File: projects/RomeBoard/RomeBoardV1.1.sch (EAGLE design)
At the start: 27 parts, among them J1 HEADER-5, J2 RASPBERRY-PI-HEADER, M1 2N7000, M2 2N7000, M3 2N7000, U1 LM1084IT-ADJ

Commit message: fixing air wire + updating library
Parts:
- M1, M2, M3: value 2N7000 -> ZVN4424A; device BrownSpaceEngineering:2N7000 -> BrownSpaceEngineering:ZVN4424A
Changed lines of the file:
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@@
 <part name="R7" library="passives" deviceset="RESISTOR" device="-PTH0.4" value="147R"/>
 <part name="GND6" library="supply1" deviceset="GND" device=""/>
-<part name="M1" library="BrownSpaceEngineering" deviceset="2N7000" device=""/>
-<part name="M2" library="BrownSpaceEngineering" deviceset="2N7000" device=""/>
-<part name="M3" library="BrownSpaceEngineering" deviceset="2N7000" device=""/>
+<part name="M1" library="BrownSpaceEngineering" deviceset="ZVN4424A" device=""/>
+<part name="M2" library="BrownSpaceEngineering" deviceset="ZVN4424A" device=""/>
+<part name="M3" library="BrownSpaceEngineering" deviceset="ZVN4424A" device=""/>
 <part name="R8" library="passives" deviceset="RESISTOR" device="-PTH0.4" value="10K"/>
 <part name="U1" library="BrownSpaceEngineering" deviceset="LM1084IT-ADJ" device=""/>
@@
 <instance part="R7" gate="G$1" x="162.56" y="48.26" rot="R90"/>
 <instance part="GND6" gate="1" x="127" y="17.78"/>
-<instance part="M1" gate="G$1" x="86.36" y="33.02"/>
-<instance part="M2" gate="G$1" x="121.92" y="33.02"/>
-<instance part="M3" gate="G$1" x="157.48" y="33.02"/>
+<instance part="M1" gate="G$1" x="86.36" y="33.02" smashed="yes">
+<attribute name="NAME" x="83.82" y="35.56" size="1.778" layer="97"/>
+<attribute name="VALUE" x="78.74" y="27.94" size="1.778" layer="97"/>
+</instance>
+<instance part="M2" gate="G$1" x="121.92" y="33.02" smashed="yes">
+<attribute name="NAME" x="119.38" y="35.56" size="1.778" layer="97"/>
+<attribute name="VALUE" x="114.3" y="27.94" size="1.778" layer="97"/>
+</instance>
+<instance part="M3" gate="G$1" x="157.48" y="33.02" smashed="yes">
+<attribute name="NAME" x="154.94" y="35.56" size="1.778" layer="97"/>
+<attribute name="VALUE" x="149.86" y="27.94" size="1.778" layer="97"/>
+</instance>
 </instances>
 <busses>

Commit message: Adding fan connectors to board, increasing board size, re-routing some stuff
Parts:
- added C4, C5: 0.1uF, BrownSpaceEngineering:CAP5MM-THRU-HOLE
- added FAN1, FAN2: FAD1-04010BBLW11, BrownSpaceEngineering:FAD1-04010BBLW11
- R2: value 450R -> 282R
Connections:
- net GND: now also C4.P$2, C5.P$2, FAN1.+\, FAN2.-
- net VIN: now also C4.P$1, C5.P$1, FAN1.-, FAN2.+\
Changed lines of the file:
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@@
 <part name="R8" library="passives" deviceset="RESISTOR" device="-PTH0.4" value="10K"/>
 <part name="U1" library="BrownSpaceEngineering" deviceset="LM1084IT-ADJ" device=""/>
-<part name="R2" library="passives" deviceset="RESISTOR" device="-PTH0.4" value="450R"/>
+<part name="R2" library="passives" deviceset="RESISTOR" device="-PTH0.4" value="282R"/>
 <part name="R1" library="passives" deviceset="RESISTOR" device="-PTH0.4" value="150R"/>
 <part name="GND2" library="supply1" deviceset="GND" device=""/>
@@
 <part name="C3" library="resistor" library_urn="urn:adsk.eagle:library:348" deviceset="CPOL-EU" device="E5-13" package3d_urn="urn:adsk.eagle:package:25855/1" value="150uF"/>
 <part name="D1" library="BrownSpaceEngineering" deviceset="1N4002" device=""/>
+<part name="FAN1" library="BrownSpaceEngineering" deviceset="FAD1-04010BBLW11" device=""/>
+<part name="FAN2" library="BrownSpaceEngineering" deviceset="FAD1-04010BBLW11" device=""/>
+<part name="GND7" library="supply1" deviceset="GND" device=""/>
+<part name="C4" library="BrownSpaceEngineering" deviceset="CAP" device="5MM-THRU-HOLE" value="0.1uF"/>
+<part name="C5" library="BrownSpaceEngineering" deviceset="CAP" device="5MM-THRU-HOLE" value="0.1uF"/>
 </parts>
 <sheets>
@@
 </segment>
 </net>
+</nets>
+</sheet>
+<sheet>
+<description>Fans</description>
+<plain>
+</plain>
+<instances>
+<instance part="FAN1" gate="G$1" x="48.26" y="48.26" smashed="yes" rot="R90">
+<attribute name="NAME" x="38.608" y="54.356" size="1.778" layer="95"/>
+<attribute name="VALUE" x="56.388" y="38.1" size="1.778" layer="96" rot="R90"/>
+</instance>
+<instance part="FAN2" gate="G$1" x="83.82" y="48.26" smashed="yes" rot="R270">
+<attribute name="NAME" x="93.472" y="57.404" size="1.778" layer="95" rot="R180"/>
+<attribute name="VALUE" x="75.692" y="58.42" size="1.778" layer="96" rot="R270"/>
+</instance>
+<instance part="GND7" gate="1" x="66.04" y="15.24"/>
+<instance part="C4" gate="G$1" x="33.02" y="45.72"/>
+<instance part="C5" gate="G$1" x="99.06" y="45.72"/>
+</instances>
+<busses>
+</busses>
+<nets>
+<net name="VIN" class="0">
+<segment>
+<pinref part="FAN1" gate="G$1" pin="-"/>
+<wire x1="48.26" y1="58.42" x2="48.26" y2="60.96" width="0.1524" layer="91"/>
+<wire x1="48.26" y1="60.96" x2="48.26" y2="71.12" width="0.1524" layer="91"/>
+<wire x1="48.26" y1="71.12" x2="30.48" y2="71.12" width="0.1524" layer="91"/>
+<wire x1="48.26" y1="71.12" x2="83.82" y2="71.12" width="0.1524" layer="91"/>
+<wire x1="83.82" y1="71.12" x2="83.82" y2="60.96" width="0.1524" layer="91"/>
+<junction x="48.26" y="71.12"/>
+<label x="33.02" y="71.12" size="1.778" layer="95"/>
+<pinref part="C4" gate="G$1" pin="P$1"/>
+<wire x1="33.02" y1="50.8" x2="33.02" y2="60.96" width="0.1524" layer="91"/>
+<wire x1="33.02" y1="60.96" x2="48.26" y2="60.96" width="0.1524" layer="91"/>
+<junction x="48.26" y="60.96"/>
+<pinref part="C5" gate="G$1" pin="P$1"/>
+<wire x1="99.06" y1="50.8" x2="99.06" y2="60.96" width="0.1524" layer="91"/>
+<wire x1="99.06" y1="60.96" x2="83.82" y2="60.96" width="0.1524" layer="91"/>
+<pinref part="FAN2" gate="G$1" pin="+\"/>
+<wire x1="83.82" y1="58.42" x2="83.82" y2="60.96" width="0.1524" layer="91"/>
+<junction x="83.82" y="60.96"/>
+</segment>
+</net>
+<net name="GND" class="0">
+<segment>
+<pinref part="FAN1" gate="G$1" pin="+\"/>
+<wire x1="48.26" y1="38.1" x2="48.26" y2="35.56" width="0.1524" layer="91"/>
+<wire x1="48.26" y1="35.56" x2="48.26" y2="22.86" width="0.1524" layer="91"/>
+<wire x1="48.26" y1="22.86" x2="66.04" y2="22.86" width="0.1524" layer="91"/>
+<wire x1="66.04" y1="22.86" x2="83.82" y2="22.86" width="0.1524" layer="91"/>
+<wire x1="83.82" y1="22.86" x2="83.82" y2="35.56" width="0.1524" layer="91"/>
+<pinref part="GND7" gate="1" pin="GND"/>
+<wire x1="66.04" y1="17.78" x2="66.04" y2="22.86" width="0.1524" layer="91"/>
+<junction x="66.04" y="22.86"/>
+<pinref part="C4" gate="G$1" pin="P$2"/>
+<wire x1="33.02" y1="43.18" x2="33.02" y2="35.56" width="0.1524" layer="91"/>
+<wire x1="33.02" y1="35.56" x2="48.26" y2="35.56" width="0.1524" layer="91"/>
+<junction x="48.26" y="35.56"/>
+<pinref part="C5" gate="G$1" pin="P$2"/>
+<wire x1="99.06" y1="43.18" x2="99.06" y2="35.56" width="0.1524" layer="91"/>
+<wire x1="99.06" y1="35.56" x2="83.82" y2="35.56" width="0.1524" layer="91"/>
+<pinref part="FAN2" gate="G$1" pin="-"/>
+<wire x1="83.82" y1="38.1" x2="83.82" y2="35.56" width="0.1524" layer="91"/>
+<junction x="83.82" y="35.56"/>
+</segment>
+</net>

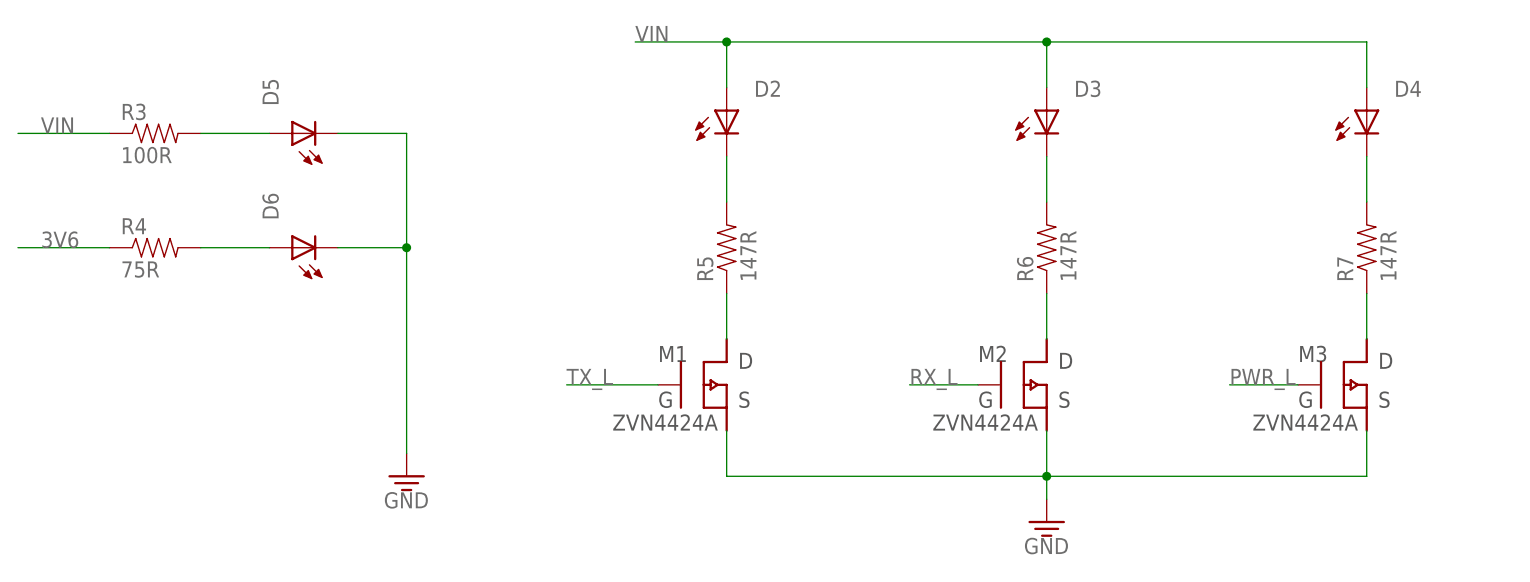
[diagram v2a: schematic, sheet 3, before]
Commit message: Adding gate pulldowns for NPNs
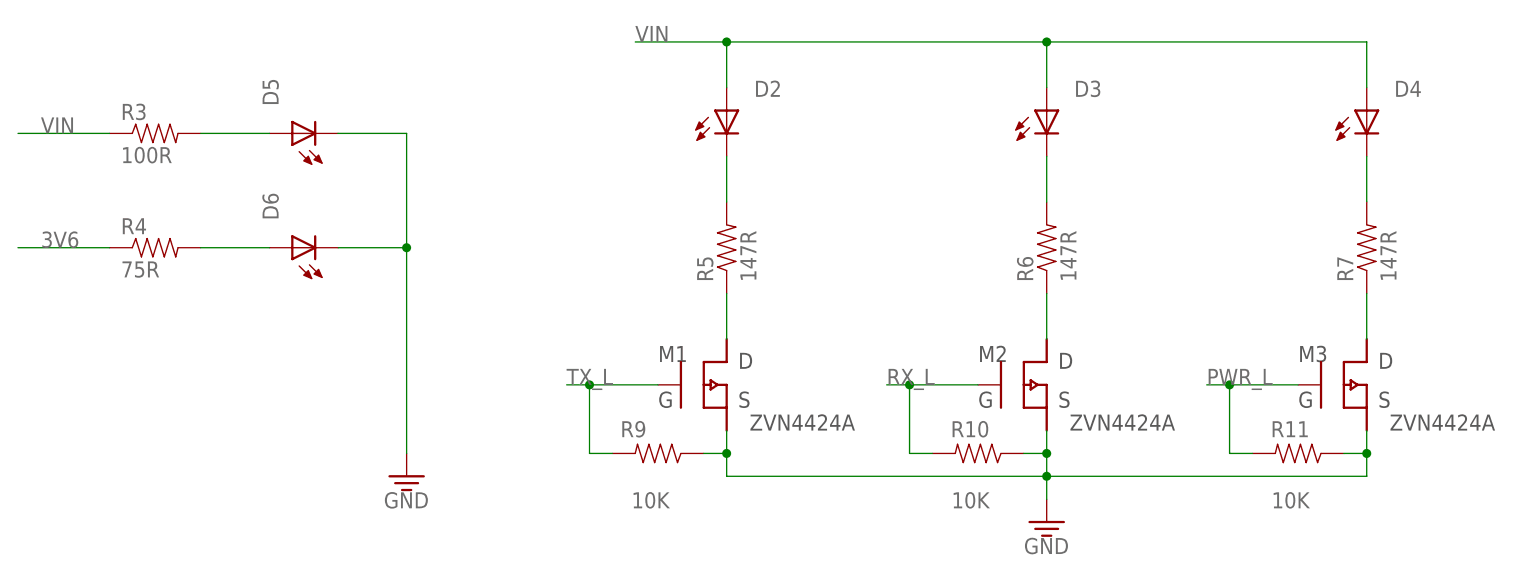
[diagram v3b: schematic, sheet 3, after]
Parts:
- added R10, R11, R9: 10K, passives:RESISTOR-PTH0.4
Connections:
- net GND: now also R10.1, R11.1, R9.1
- net PWR_L: now also R11.2
- net RX_L: now also R10.2
- net TX_L: now also R9.2
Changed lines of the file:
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@@
 <part name="C4" library="BrownSpaceEngineering" deviceset="CAP" device="5MM-THRU-HOLE" value="0.1uF"/>
 <part name="C5" library="BrownSpaceEngineering" deviceset="CAP" device="5MM-THRU-HOLE" value="0.1uF"/>
+<part name="R9" library="passives" deviceset="RESISTOR" device="-PTH0.4" value="10K"/>
+<part name="R10" library="passives" deviceset="RESISTOR" device="-PTH0.4" value="10K"/>
+<part name="R11" library="passives" deviceset="RESISTOR" device="-PTH0.4" value="10K"/>
 </parts>
 <sheets>
@@
 <instance part="M1" gate="G$1" x="86.36" y="33.02" smashed="yes">
 <attribute name="NAME" x="83.82" y="35.56" size="1.778" layer="97"/>
-<attribute name="VALUE" x="78.74" y="27.94" size="1.778" layer="97"/>
+<attribute name="VALUE" x="93.98" y="27.94" size="1.778" layer="97"/>
 </instance>
 <instance part="M2" gate="G$1" x="121.92" y="33.02" smashed="yes">
 <attribute name="NAME" x="119.38" y="35.56" size="1.778" layer="97"/>
-<attribute name="VALUE" x="114.3" y="27.94" size="1.778" layer="97"/>
+<attribute name="VALUE" x="129.54" y="27.94" size="1.778" layer="97"/>
 </instance>
 <instance part="M3" gate="G$1" x="157.48" y="33.02" smashed="yes">
 <attribute name="NAME" x="154.94" y="35.56" size="1.778" layer="97"/>
-<attribute name="VALUE" x="149.86" y="27.94" size="1.778" layer="97"/>
+<attribute name="VALUE" x="165.1" y="27.94" size="1.778" layer="97"/>
+</instance>
+<instance part="R9" gate="G$1" x="83.82" y="25.4" smashed="yes" rot="R180">
+<attribute name="NAME" x="82.55" y="28.9814" size="1.778" layer="95" rot="R180"/>
+<attribute name="VALUE" x="85.09" y="21.082" size="1.778" layer="96" rot="R180"/>
+</instance>
+<instance part="R10" gate="G$1" x="119.38" y="25.4" smashed="yes" rot="R180">
+<attribute name="NAME" x="120.65" y="28.9814" size="1.778" layer="95" rot="R180"/>
+<attribute name="VALUE" x="120.65" y="21.082" size="1.778" layer="96" rot="R180"/>
+</instance>
+<instance part="R11" gate="G$1" x="154.94" y="25.4" smashed="yes" rot="R180">
+<attribute name="NAME" x="156.21" y="28.9814" size="1.778" layer="95" rot="R180"/>
+<attribute name="VALUE" x="156.21" y="21.082" size="1.778" layer="96" rot="R180"/>
 </instance>
 </instances>
@@
 <wire x1="127" y1="22.86" x2="162.56" y2="22.86" width="0.1524" layer="91"/>
 <pinref part="M1" gate="G$1" pin="S"/>
-<wire x1="91.44" y1="27.94" x2="91.44" y2="22.86" width="0.1524" layer="91"/>
+<wire x1="91.44" y1="27.94" x2="91.44" y2="25.4" width="0.1524" layer="91"/>
 <pinref part="M2" gate="G$1" pin="S"/>
-<wire x1="127" y1="27.94" x2="127" y2="22.86" width="0.1524" layer="91"/>
+<wire x1="91.44" y1="25.4" x2="91.44" y2="22.86" width="0.1524" layer="91"/>
+<wire x1="127" y1="27.94" x2="127" y2="25.4" width="0.1524" layer="91"/>
 <pinref part="M3" gate="G$1" pin="S"/>
-<wire x1="162.56" y1="27.94" x2="162.56" y2="22.86" width="0.1524" layer="91"/>
+<wire x1="127" y1="25.4" x2="127" y2="22.86" width="0.1524" layer="91"/>
+<wire x1="162.56" y1="27.94" x2="162.56" y2="25.4" width="0.1524" layer="91"/>
+<pinref part="R10" gate="G$1" pin="1"/>
+<wire x1="162.56" y1="25.4" x2="162.56" y2="22.86" width="0.1524" layer="91"/>
+<wire x1="124.46" y1="25.4" x2="127" y2="25.4" width="0.1524" layer="91"/>
+<junction x="127" y="25.4"/>
+<pinref part="R9" gate="G$1" pin="1"/>
+<wire x1="88.9" y1="25.4" x2="91.44" y2="25.4" width="0.1524" layer="91"/>
+<junction x="91.44" y="25.4"/>
+<pinref part="R11" gate="G$1" pin="1"/>
+<wire x1="160.02" y1="25.4" x2="162.56" y2="25.4" width="0.1524" layer="91"/>
+<junction x="162.56" y="25.4"/>
 </segment>
 </net>
@@
 <segment>
 <pinref part="M1" gate="G$1" pin="G"/>
-<wire x1="83.82" y1="33.02" x2="73.66" y2="33.02" width="0.1524" layer="91"/>
+<wire x1="83.82" y1="33.02" x2="76.2" y2="33.02" width="0.1524" layer="91"/>
 <label x="73.66" y="33.02" size="1.778" layer="95"/>
+<pinref part="R9" gate="G$1" pin="2"/>
+<wire x1="78.74" y1="25.4" x2="76.2" y2="25.4" width="0.1524" layer="91"/>
+<wire x1="76.2" y1="25.4" x2="76.2" y2="33.02" width="0.1524" layer="91"/>
+<wire x1="76.2" y1="33.02" x2="73.66" y2="33.02" width="0.1524" layer="91"/>
+<junction x="76.2" y="33.02"/>
 </segment>
 </net>
@@
 <pinref part="M2" gate="G$1" pin="G"/>
 <wire x1="119.38" y1="33.02" x2="111.76" y2="33.02" width="0.1524" layer="91"/>
-<label x="111.76" y="33.02" size="1.778" layer="95"/>
+<label x="109.22" y="33.02" size="1.778" layer="95"/>
+<pinref part="R10" gate="G$1" pin="2"/>
+<wire x1="111.76" y1="33.02" x2="109.22" y2="33.02" width="0.1524" layer="91"/>
+<wire x1="114.3" y1="25.4" x2="111.76" y2="25.4" width="0.1524" layer="91"/>
+<wire x1="111.76" y1="25.4" x2="111.76" y2="33.02" width="0.1524" layer="91"/>
+<junction x="111.76" y="33.02"/>
 </segment>
 </net>
@@
 <pinref part="M3" gate="G$1" pin="G"/>
 <wire x1="154.94" y1="33.02" x2="147.32" y2="33.02" width="0.1524" layer="91"/>
-<label x="147.32" y="33.02" size="1.778" layer="95"/>
-</segment>
-</net>
+<label x="144.78" y="33.02" size="1.778" layer="95"/>
+<pinref part="R11" gate="G$1" pin="2"/>
+<wire x1="149.86" y1="25.4" x2="147.32" y2="25.4" width="0.1524" layer="91"/>
+<wire x1="147.32" y1="25.4" x2="147.32" y2="33.02" width="0.1524" layer="91"/>
+<wire x1="147.32" y1="33.02" x2="144.78" y2="33.02" width="0.1524" layer="91"/>
+<junction x="147.32" y="33.02"/>
+</segment>
+</net>

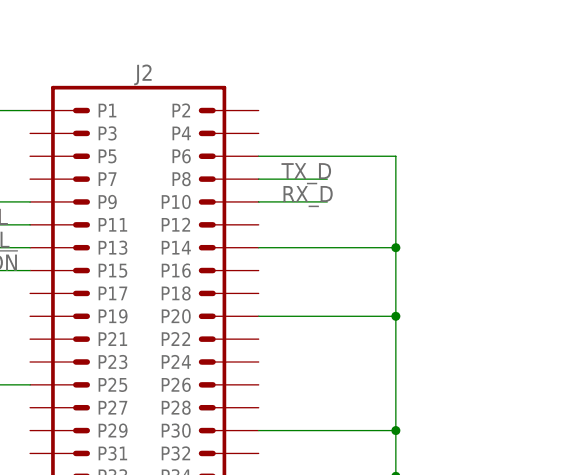
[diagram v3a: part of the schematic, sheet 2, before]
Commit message: adding vias and moving silkscreen around a bit
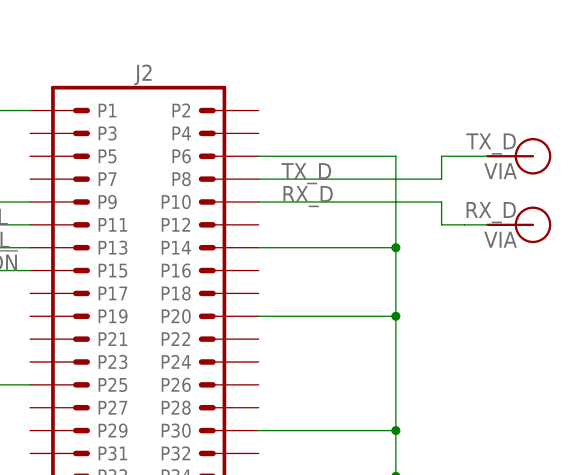
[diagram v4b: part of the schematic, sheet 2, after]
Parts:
- added V1: TX_D, BrownSpaceEngineering:VIA-120MIL
- added V2: RX_D, BrownSpaceEngineering:VIA-120MIL
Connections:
- net RX_D: now also V2.P$1
- net TX_D: now also V1.P$1
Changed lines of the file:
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@@
 <part name="R10" library="passives" deviceset="RESISTOR" device="-PTH0.4" value="10K"/>
 <part name="R11" library="passives" deviceset="RESISTOR" device="-PTH0.4" value="10K"/>
+<part name="V1" library="BrownSpaceEngineering" deviceset="VIA" device="-120MIL" value="TX_D"/>
+<part name="V2" library="BrownSpaceEngineering" deviceset="VIA" device="-120MIL" value="RX_D"/>
 </parts>
 <sheets>
@@
 <instance part="GND4" gate="1" x="220.98" y="-10.16"/>
 <instance part="R8" gate="G$1" x="104.14" y="50.8" rot="R90"/>
+<instance part="V1" gate="G$1" x="264.16" y="45.72" rot="R180"/>
+<instance part="V2" gate="G$1" x="264.16" y="38.1" rot="R180"/>
 </instances>
 <busses>
@@
 <segment>
 <pinref part="J2" gate="G$1" pin="P10"/>
-<wire x1="233.68" y1="40.64" x2="241.3" y2="40.64" width="0.1524" layer="91"/>
 <label x="236.22" y="40.64" size="1.778" layer="95"/>
+<wire x1="233.68" y1="40.64" x2="254" y2="40.64" width="0.1524" layer="91"/>
+<wire x1="254" y1="40.64" x2="254" y2="38.1" width="0.1524" layer="91"/>
+<wire x1="254" y1="38.1" x2="256.54" y2="38.1" width="0.1524" layer="91"/>
+<wire x1="256.54" y1="38.1" x2="259.08" y2="38.1" width="0.1524" layer="91"/>
+<pinref part="V2" gate="G$1" pin="P$1"/>
 </segment>
 </net>
@@
 <segment>
 <pinref part="J2" gate="G$1" pin="P8"/>
-<wire x1="233.68" y1="43.18" x2="241.3" y2="43.18" width="0.1524" layer="91"/>
 <label x="236.22" y="43.18" size="1.778" layer="95"/>
+<wire x1="233.68" y1="43.18" x2="254" y2="43.18" width="0.1524" layer="91"/>
+<wire x1="254" y1="43.18" x2="254" y2="45.72" width="0.1524" layer="91"/>
+<wire x1="254" y1="45.72" x2="259.08" y2="45.72" width="0.1524" layer="91"/>
+<pinref part="V1" gate="G$1" pin="P$1"/>
 </segment>
 </net>
